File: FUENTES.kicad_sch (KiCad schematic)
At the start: 83 parts, among them IC1 LDK320AM120R, IC11 TLV61048DBVT, J1 1604470000, Q1 FMMT491TC, U1 KF33BDT, U5 LTC3646EMSEPBF, U6 LTC3646EMSEPBF

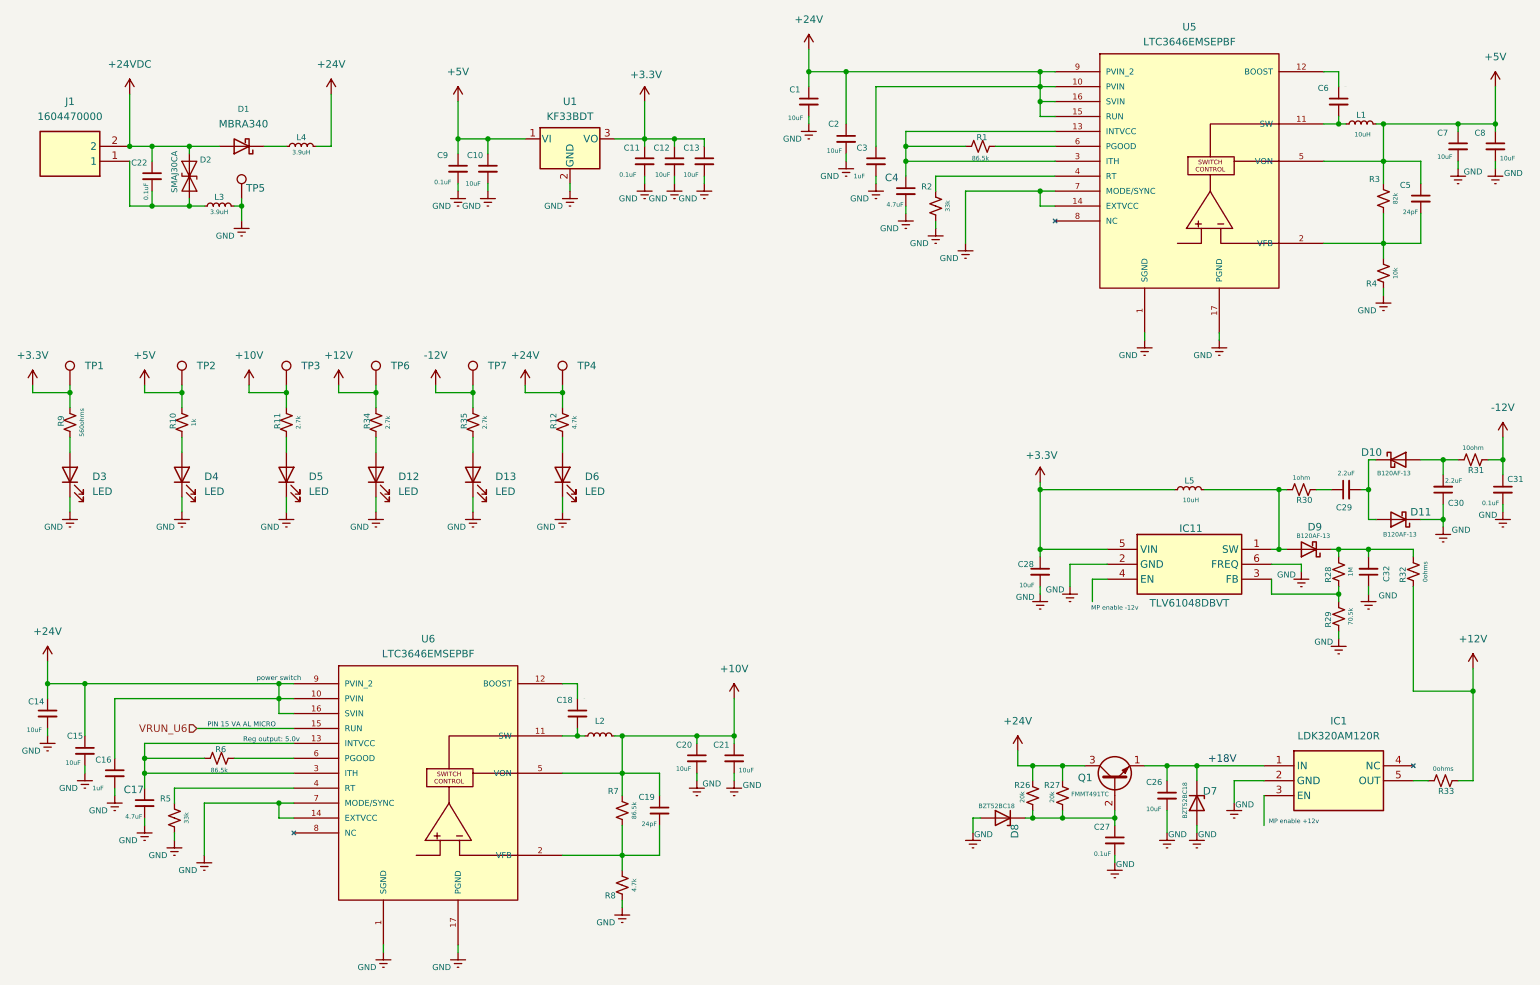
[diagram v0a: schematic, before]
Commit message: 7-may-26 346
se esta trabajando en los reles esquematico y pcb
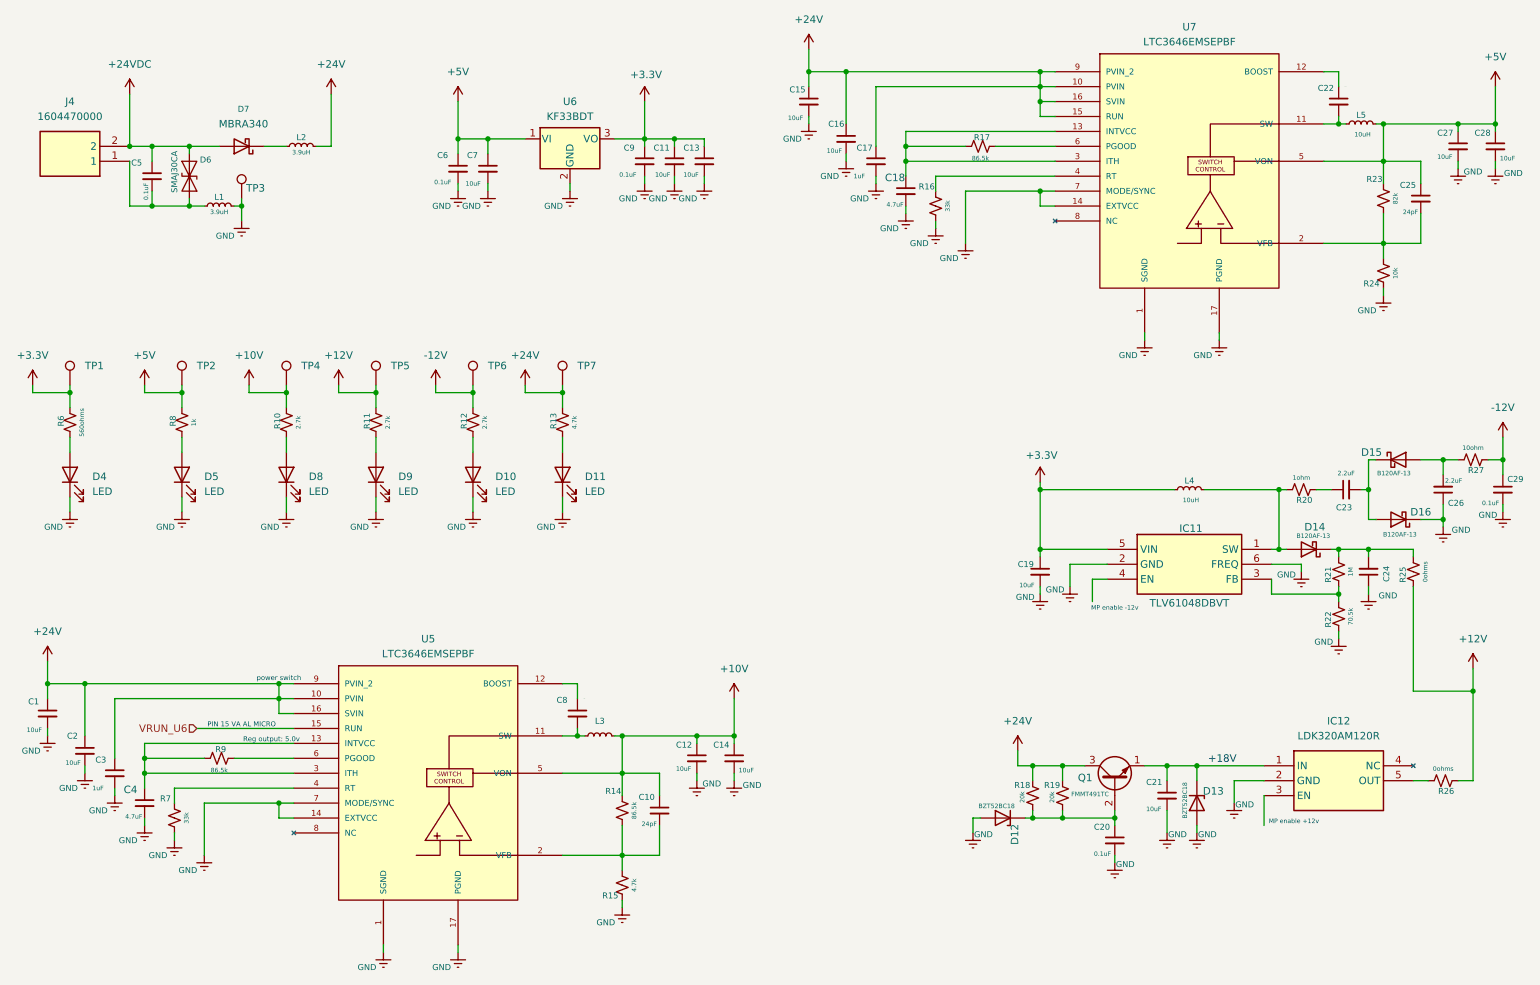
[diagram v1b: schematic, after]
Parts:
- renumbered C14 to C1, C19 to C10, C12 to C11, C20 to C12, C21 to C14, C1 to C15, C2 to C16, C3 to C17, C4 to C18, C28 to C19, C15 to C2, C27 to C20, C26 to C21, C6 to C22, C29 to C23, C32 to C24, C5 to C25, C30 to C26, C7 to C27, C8 to C28, C31 to C29, C16 to C3, C17 to C4, C22 to C5, C9 to C6, C10 to C7, C18 to C8, C11 to C9, D13 to D10, D6 to D11, D8 to D12, D7 to D13, D9 to D14, D10 to D15, D11 to D16, D3 to D4, D4 to D5, D2 to D6, D1 to D7, D5 to D8, D12 to D9, IC1 to IC12, J1 to J4, L3 to L1, L4 to L2, L2 to L3, L5 to L4, L1 to L5, R11 to R10, R34 to R11, R35 to R12, R12 to R13, R7 to R14, R8 to R15, R2 to R16, R1 to R17, R26 to R18, R27 to R19, R30 to R20, R28 to R21, R29 to R22, R3 to R23, R4 to R24, R32 to R25, R33 to R26, R31 to R27, R9 to R6, R5 to R7, R10 to R8, R6 to R9, TP5 to TP3, TP3 to TP4, TP6 to TP5, TP7 to TP6, TP4 to TP7, U6 to U5, U1 to U6, U5 to U7

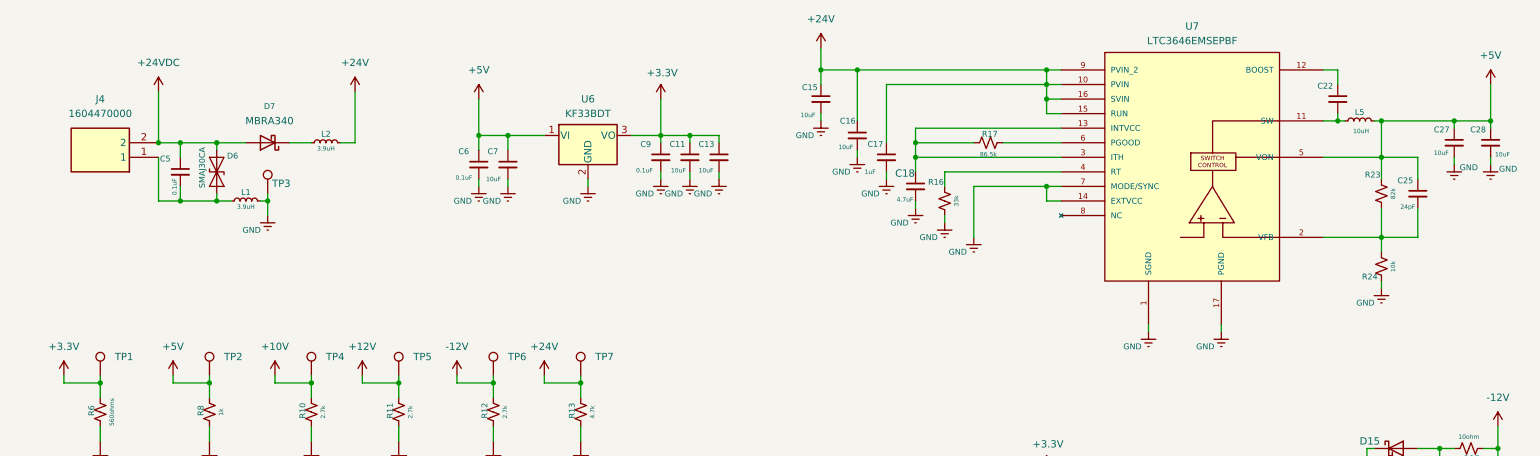
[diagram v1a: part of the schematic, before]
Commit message: 13-Mayo26 se agrego hoja de procesador y USB
hoja de USB AL 95% HOJA DEL procesador al 75%
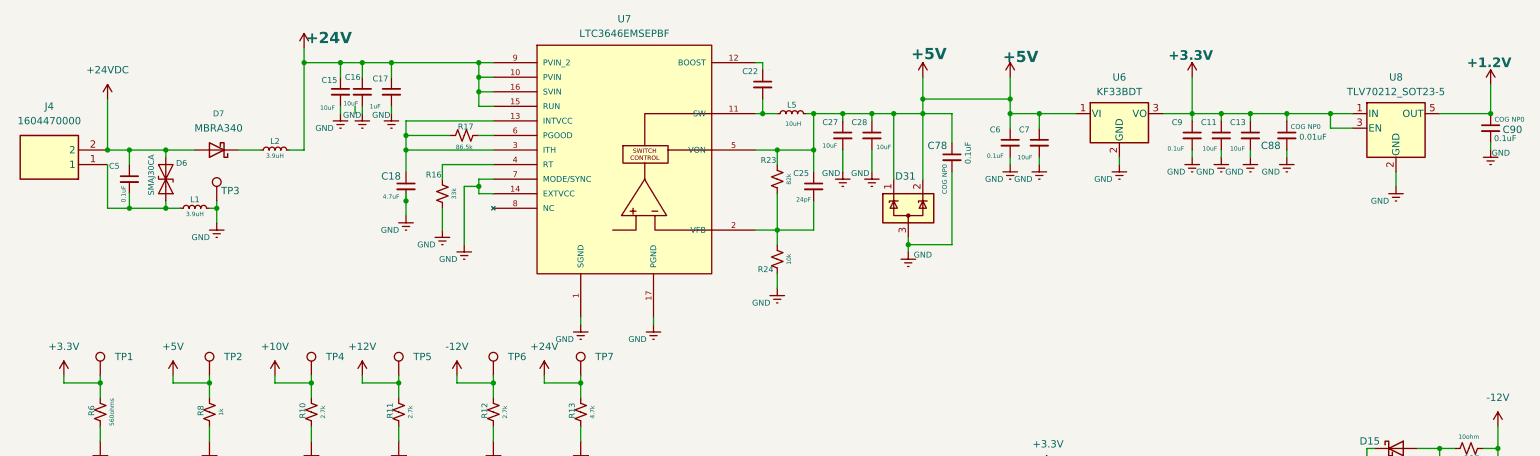
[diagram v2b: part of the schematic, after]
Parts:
- added C78, C90: 0.1uF, Capacitor_SMD:C_0603_1608Metric_Pad1.08x0.95mm_HandSolder, symbol Device:C_Small
- added C88: 0.01uF, Capacitor_SMD:C_0603_1608Metric_Pad1.08x0.95mm_HandSolder, symbol Device:C_Small
- added D31: SP0502BAHT, Package_TO_SOT_SMD:SOT-23, symbol Power_Protection:SP0502BAHT
- added U8: TLV70212_SOT23-5, Package_TO_SOT_SMD:SOT-23-5, symbol Regulator_Linear:TLV70212_SOT23-5
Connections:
- net +3.3V: now also C88.1, U8.1 (IN), U8.3 (EN)
- net +5V: now also C78.1, D31.1 (K), D31.2 (K)
- net GND: now also C78.2, C88.2, C90.2, D31.3 (A), U8.2 (GND)
- new net +1.2V: C90.1, U8.5 (OUT)
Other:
- moved on the sheet: C11, C13, C15, C16, C17, C18, C22, C25, C27, C28, C5, C6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

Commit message: 14-Mayo-26
se agregaron varias sheet de esquematico crecio al 80% la parte de esquematico
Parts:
- renumbered C8 to C10, C10 to C11, C14 to C13, C22 to C14, C25 to C15, C27 to C16, C28 to C17, C78 to C18, C6 to C19, C7 to C20, C19 to C21, C20 to C22, C21 to C23, C9 to C24, C11 to C25, C13 to C26, C88 to C27, C23 to C28, C24 to C29, C5 to C3, C26 to C30, C90 to C31, C29 to C32, C3 to C4, C4 to C5, C15 to C6, C16 to C7, C17 to C8, C18 to C9, D31 to D12, D12 to D13, D13 to D14, D14 to D15, D15 to D16, D16 to D17, D6 to D5, D5 to D6, J4 to J5, L5 to L4, L4 to L5, R11 to R10, R16 to R11, R17 to R12, R12 to R13, R13 to R14, R14 to R15, R15 to R16, R23 to R17, R24 to R18, R18 to R19, R19 to R20, R20 to R21, R21 to R22, R22 to R23, R25 to R24, R26 to R25, R27 to R26, R6 to R5, R7 to R6, R8 to R7, R9 to R8, R10 to R9, U5 to U4, U7 to U5, U8 to U7

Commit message: 15-mayo-26
15 mayo 26
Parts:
- U7: now not fitted; now left out of the parts list
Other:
- note added: "CAMBIAR A 1 AMP"
- note added: "GENERAR -12 ó -15 CON MINIMO 1AMP"
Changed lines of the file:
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@@
 		)
 	)
+	(text "GENERAR -12 ó -15 CON MINIMO 1AMP\n"
+		(exclude_from_sim no)
+		(at 229.87 105.156 0)
+		(effects
+			(font
+				(size 5.08 5.08)
+				(thickness 0.635)
+				(italic yes)
+				(color 255 0 0 1)
+			)
+		)
+	)
 	(text "PIN 15 VA AL MICRO"
 		(exclude_from_sim no)
@@
 		)
 	)
+	(text "CAMBIAR A 1 AMP\n"
+		(exclude_from_sim no)
+		(at 238.506 149.098 0)
+		(effects
+			(font
+				(size 5.08 5.08)
+				(thickness 0.635)
+				(italic yes)
+				(color 255 0 0 1)
+			)
+		)
+	)
 	(junction
 		(at 76.2 22.86)
@@
 		(at 256.54 34.29 0)
 		(unit 1)
-		(exclude_from_sim no)
-		(in_bom yes)
-		(on_board yes)
-		(dnp no)
+		(exclude_from_sim yes)
+		(in_bom no)
+		(on_board no)
+		(dnp yes)
 		(fields_autoplaced yes)
 		(property "Reference" "U7"

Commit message: pcb 18 may 26
 falta poner la fuente de +12/ ya esta casi todo
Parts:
- added F2, F3: Fuse, symbol Device:Fuse
- U5: value LTC3646EMSEPBF -> LTC3646E
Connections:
- net +3.3V: now also F2.1, F3.1
- new net +3.3v_Fuse: F2.2
- new net +3.3v_Fuse_comm: F3.2
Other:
- moved on the sheet: C14, C15, C16, C17, C18, C9, D10, D11, D12, D4, D6, D7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

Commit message: 22 mayo 26 actualizacion
se actualizo la PCB para la rama laptop Antigua
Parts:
- removed L2: 3.9uH, INDUCTORES GRACIDA:INDM4532X320N, symbol Device:L_Small
- added C11, C12: 2.2uF, Capacitor_THT:C_Rect_L26.5mm_W11.5mm_P22.50mm_MKS4, symbol Device:C_Small
- added C21, C24: 1500pF, Capacitor_THT:C_Disc_D9.0mm_W5.0mm_P10.00mm, symbol Device:C_Small
- added F1, F2, F3: Fuse, symbol Device:Fuse
- added L25: SDR0906-3R9ML, Inductores_GSI:SDR0906-3R9ML, symbol INDUCTORES_GSI:SDR0906-3R9ML
- added L4: 4.7uH, Inductor_SMD:L_0805_2012Metric_Pad1.15x1.40mm_HandSolder, symbol Device:L_Small
- added PS1: REC15E-2412DZ, Fuentes_GSI:REC15E-2412DZ, symbol Fuentes_GSI:REC15E-2412DZ
- added PS2: MGFW402412, Fuentes_GSI:MGFW400512, symbol Fuentes GSI:MGFW402412
- C30: renamed from C21; now not fitted; now left out of the parts list
- C31: renamed from C22; now not fitted; now left out of the parts list
- C32: renamed from C23; now not fitted; now left out of the parts list
- C33: renamed from C28; now not fitted; now left out of the parts list
- C34: renamed from C29; now not fitted; now left out of the parts list
- C35: renamed from C30; now not fitted; now left out of the parts list
- C36: renamed from C32; now not fitted; now left out of the parts list
- D13, D14, D15, D16, D17: now not fitted; now left out of the parts list
- IC1: renamed from IC11; now not fitted; now left out of the parts list
- IC2: renamed from IC12; now not fitted; now left out of the parts list
- L6: renamed from L5; now not fitted; now left out of the parts list
- Q1: footprint Package_TO_SOT_SMD:TSOT-23_HandSoldering -> Package_TO_SOT_THT:TO-18-3; now not fitted; now left out of the parts list
- R21: renamed from R19; now not fitted; now left out of the parts list
- R22: renamed from R20; now not fitted; now left out of the parts list
- R23: renamed from R21; now not fitted; now left out of the parts list
- R24: renamed from R22; now not fitted; now left out of the parts list
- R25: renamed from R23; now not fitted; now left out of the parts list
- R26: renamed from R24; now not fitted; now left out of the parts list
- R27: renamed from R25; now not fitted; now left out of the parts list
- R28: renamed from R26; now not fitted; now left out of the parts list
- renumbered C11 to C13, C12 to C14, C14 to C15, C15 to C16, C13 to C17, C16 to C18, C17 to C19, C18 to C20, C19 to C22, C20 to C23, C24 to C25, C25 to C26, C26 to C27, C27 to C28, C31 to C29, D6 to D5, D5 to D6, D8 to D7, D7 to D8, F2 to F4, F3 to F5, J5 to J4, L4 to L5, R6 to R10, R8 to R11, R10 to R12, R11 to R14, R12 to R15, R14 to R16, R15 to R17, R16 to R18, R17 to R19, R18 to R20, R5 to R7, R7 to R8, TP4 to TP3, TP3 to TP4, U5 to U2, U4 to U21, U6 to U3, U7 to U4
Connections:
- net +24V: now also F1.1, F2.1, L25.4
- net at D8.1 (K): now also L25.1
- net GND renamed -12V_Analog
- net -12V_Analog: now also C11.2, C12.2, C21.1, F3.2, PS1.2 (-Vin)
- new net: C11.1, C12.1, F1.2, F2.2, L4.1
- new net: C24.1, L4.2, PS1.1 (+Vin)
- new net: C21.2, PS1.4 (-Vo)
- new net +12V_Analog: PS1.6 (+Vo)
- new net AGND: C24.2, F3.1, PS1.5 (Com)
- no-connect marks 0 -> 1
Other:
- note removed: "GENERAR -12 ó -15 CON MINIMO 1AMP"

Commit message: 26-05-26
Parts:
- removed C30, C32: 10uF, Capacitor_SMD:C_0603_1608Metric_Pad1.08x0.95mm_HandSolder, symbol Device:C_Small
- removed C31, C36: 0.1uF, Capacitor_SMD:C_0603_1608Metric_Pad1.08x0.95mm_HandSolder, symbol Device:C_Small
- removed C33, C35: 2.2uF, Capacitor_SMD:C_0603_1608Metric_Pad1.08x0.95mm_HandSolder, symbol Device:C_Small
- removed C34: 2.2uF 25v 0603, Capacitor_SMD:C_0603_1608Metric_Pad1.08x0.95mm_HandSolder, symbol Device:C_Small
- removed D13, D14: BZT52BC18, Diode_SMD:D_SOD-123F, symbol Diode:BZT52Bxx
- removed D15, D16, D17: B120AF-13, Diode_SMD:D_SMA, symbol Diode:B120-E3
- removed IC1: TLV61048DBVT, Package_TO_SOT_SMD:TSOT-23-6_HandSoldering, symbol REGULADORES_GRACDA:TLV61048DBVT
- removed IC2: LDK320AM120R, Package_TO_SOT_SMD:SOT-23-5, symbol REGULADORES_GRACDA:LDK320AM120R
- removed L6: 10uH, INDUCTORES GRACIDA:744065100, symbol Device:L_Small
- removed Q1: FMMT491TC, Package_TO_SOT_THT:TO-18-3, symbol Transistor_BJT:BC108
- removed R21, R22: 20k, Resistor_SMD:R_0603_1608Metric_Pad0.98x0.95mm_HandSolder, symbol Device:R_Small_US
- removed R23: 1ohm, Resistor_SMD:R_0603_1608Metric_Pad0.98x0.95mm_HandSolder, symbol Device:R_Small_US
- removed R24: 1M, Resistor_SMD:R_0603_1608Metric_Pad0.98x0.95mm_HandSolder, symbol Device:R_Small_US
- removed R25: 70.5k, Resistor_SMD:R_0603_1608Metric_Pad0.98x0.95mm_HandSolder, symbol Device:R_Small_US
- removed R26, R27: 0ohms, Resistor_SMD:R_0603_1608Metric_Pad0.98x0.95mm_HandSolder, symbol Device:R_Small_US
- removed R28: 10ohm, Resistor_SMD:R_0603_1608Metric_Pad0.98x0.95mm_HandSolder, symbol Device:R_Small_US
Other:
- note removed: "+18V"
- note removed: "CAMBIAR A 1 AMP"
- note removed: "MP enable +12v"
- note removed: "MP enable -12v"
- moved on the sheet: D10, D4, D5, D7, D9, R12, R13, R7, R8, R9, TP1, TP2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
